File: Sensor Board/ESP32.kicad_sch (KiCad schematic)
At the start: 33 parts, among them Q1 SS8050-G, Q2 SS8050-G, SW1 SW_Push, SW2 SW_Push, U1 AZ1117-3.3, U2 ESP32-S3-WROOM-1-N16R2

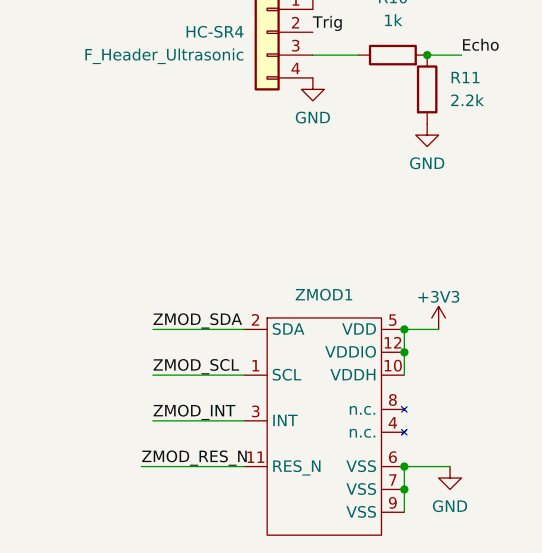
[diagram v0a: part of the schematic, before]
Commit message: Added I2C resistors
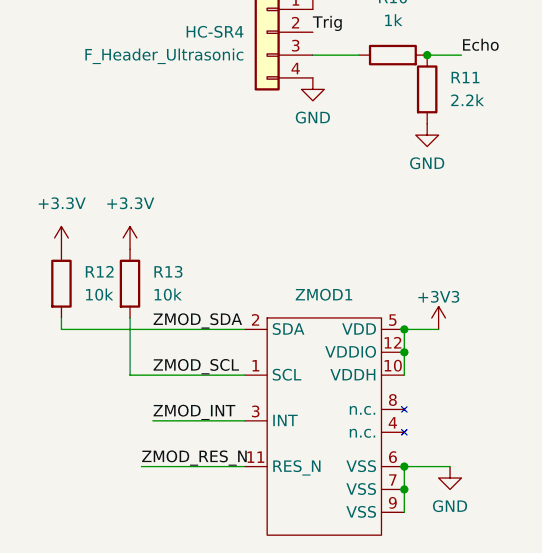
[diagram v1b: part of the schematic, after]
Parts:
- added R12, R13: 10k, symbol Device:R
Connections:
- net ZMOD_SCL: now also R13.2
- net ZMOD_SDA: now also R12.2
- new net +3.3V: R12.1, R13.1
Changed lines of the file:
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@@
-    (stroke (width 0) (type default))
-  )
-  (wire (pts (xy 31.75 167.64) (xy 41.91 167.64))
     (stroke (width 0) (type default))
   )
@@
     (stroke (width 0) (type default))
   )
-  (wire (pts (xy 31.75 172.72) (xy 41.91 172.72))
+  (wire (pts (xy 29.21 172.72) (xy 41.91 172.72))
     (stroke (width 0) (type default))
   )
@@
     (stroke (width 0) (type default))
   )
+  (wire (pts (xy 21.59 166.37) (xy 21.59 167.64))
+    (stroke (width 0) (type default))
+  )
   (wire (pts (xy 198.12 62.23) (xy 203.2 62.23))
     (stroke (width 0) (type default))
@@
     (stroke (width 0) (type default))
   )
+  (wire (pts (xy 29.21 166.37) (xy 29.21 172.72))
+    (stroke (width 0) (type default))
+  )
   (wire (pts (xy 87.63 86.36) (xy 64.77 86.36))
     (stroke (width 0) (type default))
@@
   )
   (wire (pts (xy 87.63 101.6) (xy 90.17 101.6))
+    (stroke (width 0) (type default))
+  )
+  (wire (pts (xy 21.59 167.64) (xy 41.91 167.64))
     (stroke (width 0) (type default))
   )
@@
   (label "CHIP_PU" (at 195.58 46.99 180) (fields_autoplaced)
     (effects (font (size 1.27 1.27)) (justify right bottom))
+  )
+  (symbol (lib_id "power:+3.3V") (at 29.21 158.75 0) (unit 1)
+    (in_bom yes) (on_board yes) (dnp no) (fields_autoplaced)
+    (property "Reference" "#PWR029" (at 29.21 162.56 0)
+      (effects (font (size 1.27 1.27)) hide)
+    )
+    (property "Value" "+3.3V" (at 29.21 153.67 0)
+      (effects (font (size 1.27 1.27)))
+    )
+    (property "Footprint" "" (at 29.21 158.75 0)
+      (effects (font (size 1.27 1.27)) hide)
+    )
+    (property "Datasheet" "" (at 29.21 158.75 0)
+      (effects (font (size 1.27 1.27)) hide)
+    )
+    (pin "1")
+    (instances
+      (project "ESP32"
+        (path "/668738a4-4fba-4c81-8219-00fa4ae32623"
+          (reference "#PWR029") (unit 1)
+        )
+      )
+    )
   )
   (symbol (lib_id "basic:C") (at 168.91 50.8 0) (unit 1)
@@
     )
   )
+  (symbol (lib_id "Device:R") (at 29.21 162.56 0) (unit 1)
+    (in_bom yes) (on_board yes) (dnp no) (fields_autoplaced)
+    (property "Reference" "R13" (at 31.75 161.29 0)
+      (effects (font (size 1.27 1.27)) (justify left))
+    )
+    (property "Value" "10k" (at 31.75 163.83 0)
+      (effects (font (size 1.27 1.27)) (justify left))
+    )
+    (property "Footprint" "" (at 27.432 162.56 90)
+      (effects (font (size 1.27 1.27)) hide)
+    )
+    (property "Datasheet" "~" (at 29.21 162.56 0)
+      (effects (font (size 1.27 1.27)) hide)
+    )
+    (pin "2")
+    (pin "1")
+    (instances
+      (project "ESP32"
+        (path "/668738a4-4fba-4c81-8219-00fa4ae32623"
+          (reference "R13") (unit 1)
+        )
+      )
+    )
+  )
   (symbol (lib_id "power:+5V") (at 130.81 132.08 0) (unit 1)
     (in_bom yes) (on_board yes) (dnp no) (fields_autoplaced)
@@
         (path "/668738a4-4fba-4c81-8219-00fa4ae32623"
           (reference "C4") (unit 1)
+        )
+      )
+    )
+  )
+  (symbol (lib_id "Device:R") (at 21.59 162.56 0) (unit 1)
+    (in_bom yes) (on_board yes) (dnp no) (fields_autoplaced)
+    (property "Reference" "R12" (at 24.13 161.29 0)
+      (effects (font (size 1.27 1.27)) (justify left))
+    )
+    (property "Value" "10k" (at 24.13 163.83 0)
+      (effects (font (size 1.27 1.27)) (justify left))
+    )
+    (property "Footprint" "" (at 19.812 162.56 90)
+      (effects (font (size 1.27 1.27)) hide)
+    )
+    (property "Datasheet" "~" (at 21.59 162.56 0)
+      (effects (font (size 1.27 1.27)) hide)
+    )
+    (pin "2")
+    (pin "1")
+    (instances
+      (project "ESP32"
+        (path "/668738a4-4fba-4c81-8219-00fa4ae32623"
+          (reference "R12") (unit 1)
         )
       )
@@
         )
       )
+    )
+  )
+  (symbol (lib_id "power:+3.3V") (at 21.59 158.75 0) (unit 1)
+    (in_bom yes) (on_board yes) (dnp no) (fields_autoplaced)
+    (property "Reference" "#PWR028" (at 21.59 162.56 0)
+      (effects (font (size 1.27 1.27)) hide)
+    )
+    (property "Value" "+3.3V" (at 21.59 153.67 0)
+      (effects (font (size 1.27 1.27)))
+    )
+    (property "Footprint" "" (at 21.59 158.75 0)
+      (effects (font (size 1.27 1.27)) hide)
+    )
+    (property "Datasheet" "" (at 21.59 158.75 0)
+      (effects (font (size 1.27 1.27)) hide)
+    )
+    (pin "1")
+    (instances
+      (project "ESP32"
+        (path "/668738a4-4fba-4c81-8219-00fa4ae32623"
+          (reference "#PWR028") (unit 1)
+        )
+      )
